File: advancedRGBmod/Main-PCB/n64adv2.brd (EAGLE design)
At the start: 67.3 x 91.2 mm, 158 parts, among them U1 10CL025YE144, U2 ADV7513, U3 S25FLXXXSO8-DUAL, U4 27M, U5 TLV70212DBVT, U6 TLV70225DBVT, U7 TLV70218DBVT, U8 TLV70033, X1 FH12-24S-0.5SH, X3 hdmi-con

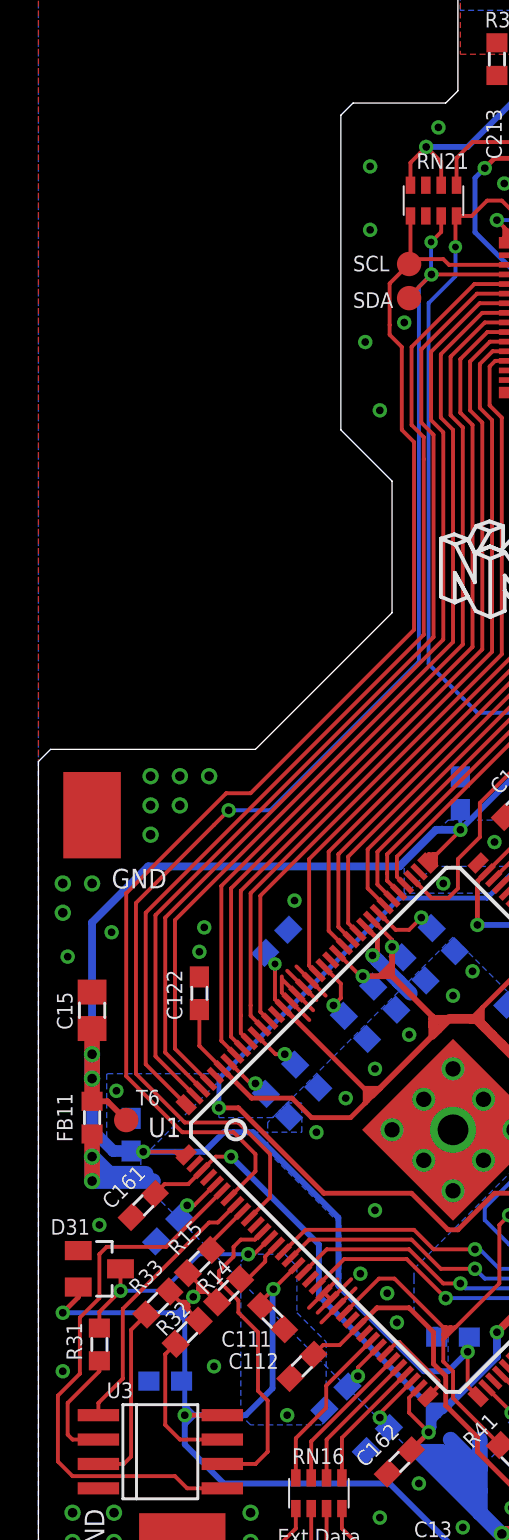
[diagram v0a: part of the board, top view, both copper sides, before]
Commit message: modify outline layer a bit
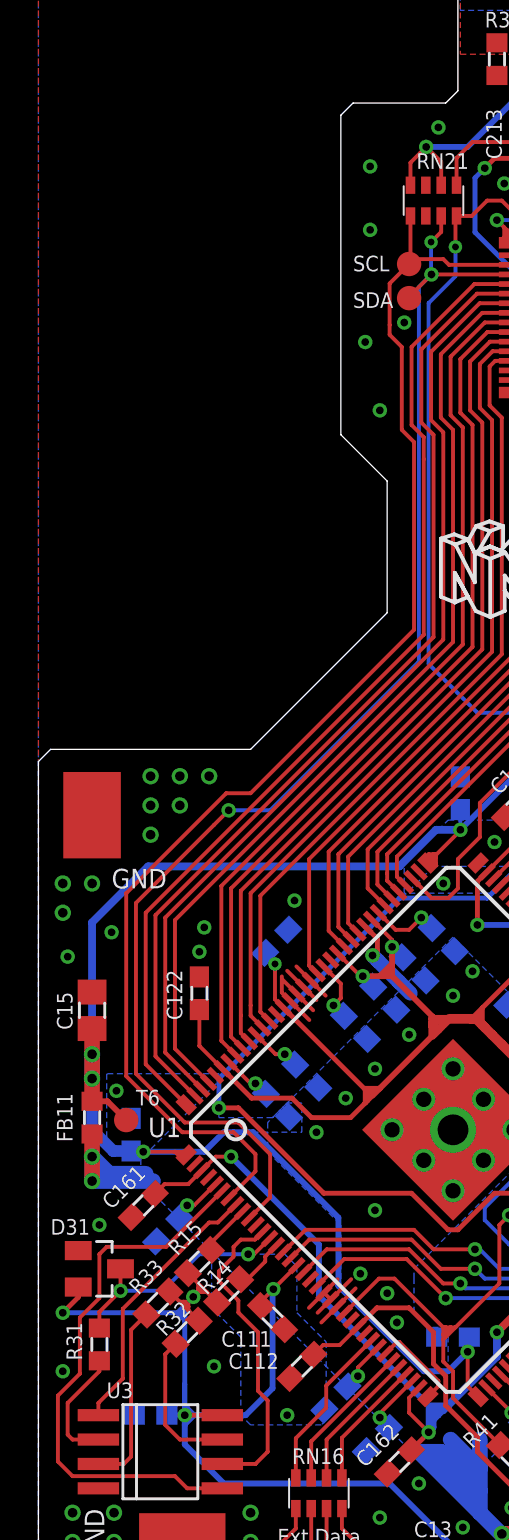
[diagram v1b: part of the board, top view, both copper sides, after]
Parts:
- moved C31 1.93 mm to (5.84, 9.14)
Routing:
- net VCCIO: track 508.6 -> 511.1 mm
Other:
- outline, holes or cut-outs redrawn
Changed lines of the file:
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@@
 <wire x1="0.635" y1="0" x2="0" y2="0.635" width="0" layer="20"/>
 <wire x1="0" y1="0.635" x2="0" y2="43.18" width="0" layer="20"/>
-<wire x1="11.303" y1="43.815" x2="18.415" y2="50.927" width="0" layer="20"/>
-<wire x1="18.415" y1="50.927" x2="18.415" y2="57.785" width="0" layer="20"/>
+<wire x1="11.049" y1="43.815" x2="18.161" y2="50.927" width="0" layer="20"/>
+<wire x1="18.161" y1="50.927" x2="18.161" y2="57.785" width="0" layer="20"/>
 <wire x1="21.844" y1="90.551" x2="22.479" y2="91.186" width="0" layer="20"/>
 <wire x1="22.479" y1="91.186" x2="44.196" y2="91.186" width="0" layer="20"/>
@@
 <wire x1="41.783" y1="4.826" x2="41.783" y2="0.635" width="0" layer="20"/>
 <wire x1="41.783" y1="0.635" x2="41.148" y2="0" width="0" layer="20"/>
-<wire x1="11.303" y1="43.815" x2="0.635" y2="43.815" width="0" layer="20"/>
+<wire x1="11.049" y1="43.815" x2="0.635" y2="43.815" width="0" layer="20"/>
 <wire x1="0.635" y1="43.815" x2="0" y2="43.18" width="0" layer="20"/>
 <dimension x1="64.77" y1="41.783" x2="64.77" y2="53.467" x3="77.724" y3="47.625" textsize="1.27" textratio="15" layer="51"/>
@@
 <wire x1="44.831" y1="90.551" x2="44.196" y2="91.186" width="0" layer="20"/>
 <wire x1="44.831" y1="90.551" x2="44.831" y2="78.105" width="0" layer="20"/>
-<wire x1="18.415" y1="57.785" x2="15.748" y2="60.452" width="0" layer="20"/>
-<wire x1="15.748" y1="60.452" x2="15.748" y2="76.835" width="0" layer="20"/>
+<wire x1="18.161" y1="57.785" x2="15.748" y2="60.198" width="0" layer="20"/>
+<wire x1="15.748" y1="60.198" x2="15.748" y2="76.835" width="0" layer="20"/>
 <rectangle x1="31.5595" y1="6.2865" x2="33.401" y2="7.62" layer="25"/>
 <text x="60.198" y="80.772" size="1.016" layer="25" font="vector" ratio="15">D1</text>
@@
 <attribute name="NAME" x="29.083" y="73.787" size="0.8128" layer="25" font="vector" ratio="15" rot="R90"/>
 </element>
-<element name="C31" library="rcl" package="C0603" value="0.1u" x="6.604" y="10.922" smashed="yes" rot="MR0">
-<attribute name="NAME" x="7.493" y="11.938" size="0.8128" layer="26" font="vector" ratio="15" rot="MR0"/>
+<element name="C31" library="rcl" package="C0603" value="0.1u" x="5.842" y="9.144" smashed="yes" rot="MR0">
+<attribute name="NAME" x="6.731" y="10.16" size="0.8128" layer="26" font="vector" ratio="15" rot="MR0"/>
 </element>
 <element name="C41" library="rcl" package="C0603" value="0.01u" x="35.306" y="6.35" smashed="yes" rot="R270">
@@
 <wire x1="7.62" y1="9.144" x2="7.62" y2="9.652" width="0.254" layer="16"/>
 <wire x1="7.62" y1="9.652" x2="7.62" y2="10.756" width="0.254" layer="16"/>
-<wire x1="7.62" y1="10.756" x2="7.454" y2="10.922" width="0.254" layer="16"/>
+<wire x1="7.62" y1="8.978" x2="7.454" y2="9.144" width="0.254" layer="16"/>
 <wire x1="7.62" y1="9.144" x2="7.874" y2="9.144" width="0.3048" layer="16"/>
 <wire x1="7.874" y1="9.144" x2="8.128" y2="9.144" width="0.3048" layer="16"/>
@@
 <wire x1="22.86" y1="8.001" x2="21.209" y2="9.652" width="0.254" layer="1"/>
 <wire x1="21.209" y1="9.652" x2="21.209" y2="11.176" width="0.254" layer="1"/>
+<wire x1="7.62" y1="10.756" x2="7.62" y2="8.978" width="0.254" layer="16"/>
+<wire x1="7.454" y1="9.144" x2="6.692" y2="9.144" width="0.254" layer="16"/>
 </signal>
 <signal name="VCCA">
@@
 <wire x1="53.0895" y1="16.958" x2="53.34" y2="17.2085" width="0.254" layer="1"/>
 <polygon width="0.2032" layer="16">
-<vertex x="10.541" y="13.208"/>
-<vertex x="10.541" y="17.145"/>
-<vertex x="10.922" y="17.526"/>
+<vertex x="9.017" y="14.732"/>
+<vertex x="9.017" y="17.526"/>
 <vertex x="12.827" y="17.526"/>
 <vertex x="13.462" y="16.891"/>
@@
 <vertex x="11.049" y="8.636"/>
 <vertex x="10.541" y="9.144"/>
+<vertex x="10.541" y="13.208"/>
 </polygon>
 <via x="36.576" y="15.748" extent="1-16" drill="0.4"/>

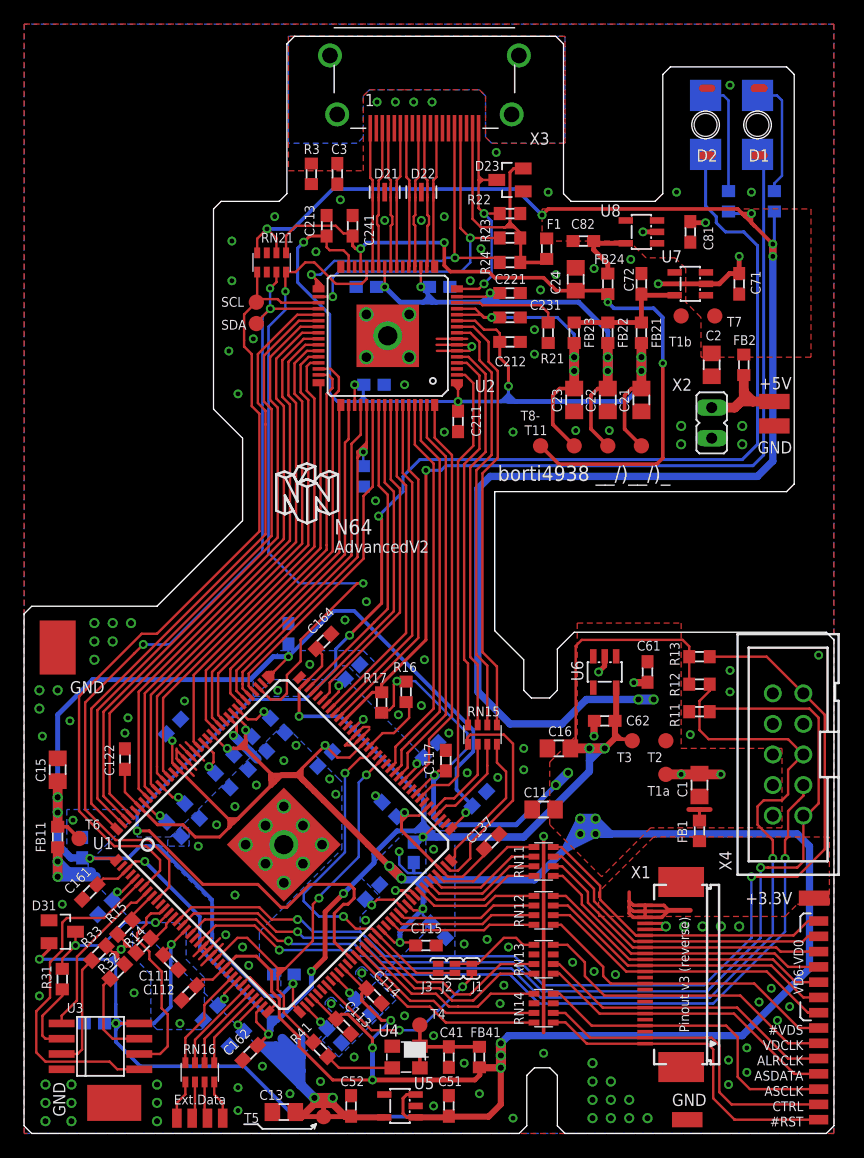
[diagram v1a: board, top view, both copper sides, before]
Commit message: remove connections for DE and MCLK and change pinout for system LEDs
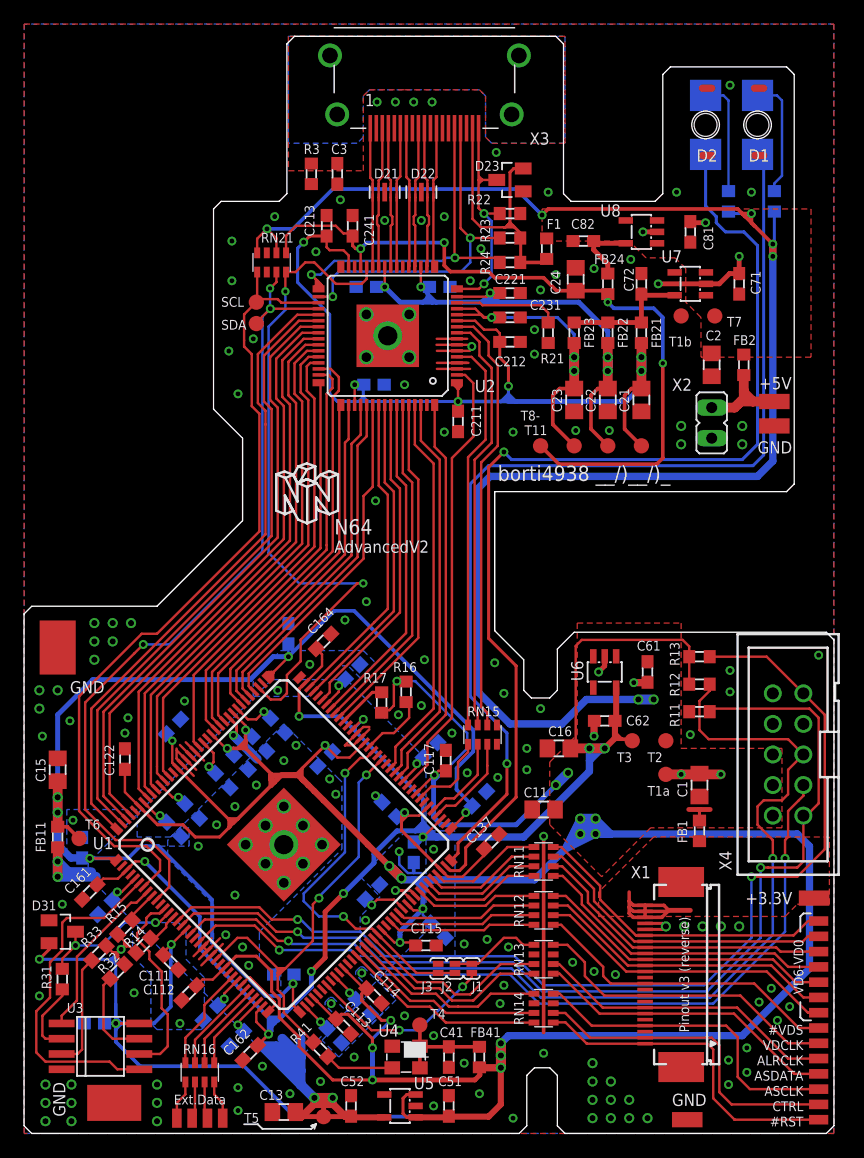
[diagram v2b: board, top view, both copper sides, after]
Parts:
- removed R25: 50, rcl:R0603
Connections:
- removed net N$26: U1.85, U2.63
- removed net N$29: RN15.4, U2.4
- removed net N$56: RN15.8, U1.72
- new net N$15: D1.C, U1.72
- net GND: now also U2.4, U2.63; no longer R25.2
- net N$11: now also U1.80; no longer U1.71
- net N$13: now also U1.71; no longer U1.49
- net N$27: now also U1.85; no longer U1.83
- net N$28: now also U1.83; no longer U1.80
- net N$30: now also RN15.4; no longer RN15.3
- net N$31: now also RN15.3; no longer RN15.2
- net N$32: now also RN15.2; no longer RN15.1
- net N$62: no longer D1.C
- net TX_CLK: no longer R25.1
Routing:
- net N$15: track 0.00 -> 85.0 mm, vias 0 -> 1
- net N$62: track 77.9 -> 4.18 mm, vias 1 -> 0
- net N$13: track 127.8 -> 88.2 mm, vias 3 -> 1
- net N$26: track 33.2 -> 0.00 mm
- net N$29: track 32.0 -> 0.00 mm
- net N$56: track 11.9 -> 0.00 mm
- net N$11: track 18.4 -> 7.04 mm
- net TX_CLK: track 33.1 -> 28.7 mm, vias 1 -> 0
- net N$28: track 38.7 -> 37.3 mm
- net N$27: track 33.7 -> 32.9 mm
- net GND: track 97.8 -> 97.1 mm, vias 171 -> 174
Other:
- board text added: "N64Av2_20181111"
- board text removed: "N64Av2_20180913"
